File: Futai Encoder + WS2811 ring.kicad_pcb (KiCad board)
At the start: 2 copper layers, 31 x 49 mm, 41 parts, among them J1 Conn_02x05_Top_Bottom, SW1 RotaryEncoder_Switch_RGB

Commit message: new 3d for encoder, fixing ibom.html + new images
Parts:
- C1, C10, C4, C7: value 33n -> 100n

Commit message: adding v0.7
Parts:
- added kibuzzard-61E72360: G***, kibuzzard-61E72360, B.Cu at (148.6, 99.2)
- D1, D10, D11, D12, D2, D3, D4, D5, D6, D7, D8, D9: footprint footprints:WS2811-THT-LED -> andilge KiCad footprints:WS2811D-F5-1261
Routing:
- net Net-(D11-Pad2): track 5.51 -> 4.10 mm
- net Net-(D3-Pad2): track 7.47 -> 6.39 mm
- net Net-(D8-Pad2): track 8.51 -> 7.45 mm
- net Net-(D9-Pad2): track 7.63 -> 6.60 mm
- net +5V: track 154.3 -> 153.6 mm
- net ENC_A: track 28.4 -> 27.8 mm
- net ENC_B: track 43.4 -> 42.8 mm
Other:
- board text added: "v0.7"
- board text removed: "by andilge"
- board text removed: "v0.65"

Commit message: adding fabrication files for 0.7
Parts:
- D1, D10, D11, D12, D2, D3, D4, D5, D6, D7, D8, D9: value WS2812D -> WS2812D F5 hat

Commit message: lowering value for R1-R12
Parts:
- R1, R10, R11, R12, R2, R3, R4, R5, R6, R7, R8, R9: value 130 -> 68
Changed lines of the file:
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@@
       (drillshape 0)
       (scaleselection 1)
-      (outputdirectory "gerber-and-bom/")
+      (outputdirectory "fabrication/")
     )
   )
@@
     (descr "Through hole straight pin header, 1x03, 2.54mm pitch, single row")
     (tags "Through hole pin header THT 1x03 2.54mm single row")
-    (property "Purchse" "https://www.aliexpress.com/item/32790928817.html")
+    (property "Purchase" "https://www.aliexpress.com/item/32790928817.html")
     (property "Sheetfile" "Futai Encoder + WS2811 ring.kicad_sch")
     (property "Sheetname" "")
@@
     (descr "Through hole straight pin header, 1x03, 2.54mm pitch, single row")
     (tags "Through hole pin header THT 1x03 2.54mm single row")
-    (property "Purchse" "https://www.aliexpress.com/item/32790928817.html")
+    (property "Purchase" "https://www.aliexpress.com/item/32790928817.html")
     (property "Sheetfile" "Futai Encoder + WS2811 ring.kicad_sch")
     (property "Sheetname" "")
@@
       (effects (font (size 1 1) (thickness 0.15)) (justify mirror))
     )
-    (fp_text value "130" (at 0 -1.65 90) (layer "B.Fab")
+    (fp_text value "68" (at 0 -1.65 90) (layer "B.Fab")
       (effects (font (size 1 1) (thickness 0.15)) (justify mirror))
     )
@@
       (effects (font (size 1 1) (thickness 0.15)) (justify mirror))
     )
-    (fp_text value "130" (at 0 -1.65) (layer "B.Fab")
+    (fp_text value "68" (at 0 -1.65) (layer "B.Fab")
       (effects (font (size 1 1) (thickness 0.15)) (justify mirror))
     )
@@
       (effects (font (size 1 1) (thickness 0.15)) (justify mirror))
     )
-    (fp_text value "130" (at 0 -1.65 90) (layer "B.Fab")
+    (fp_text value "68" (at 0 -1.65 90) (layer "B.Fab")
       (effects (font (size 1 1) (thickness 0.15)) (justify mirror))
     )
@@
       (effects (font (size 1 1) (thickness 0.15)) (justify mirror))
     )
-    (fp_text value "130" (at 0 -1.65 270) (layer "B.Fab")
+    (fp_text value "68" (at 0 -1.65 270) (layer "B.Fab")
       (effects (font (size 1 1) (thickness 0.15)) (justify mirror))
     )
@@
       (effects (font (size 1 1) (thickness 0.15)) (justify mirror))
     )
-    (fp_text value "130" (at 0 -1.65 180) (layer "B.Fab")
+    (fp_text value "68" (at 0 -1.65 180) (layer "B.Fab")
       (effects (font (size 1 1) (thickness 0.15)) (justify mirror))
     )
@@
       (effects (font (size 1 1) (thickness 0.15)) (justify mirror))
     )
-    (fp_text value "130" (at 0 -1.65 90) (layer "B.Fab")
+    (fp_text value "68" (at 0 -1.65 90) (layer "B.Fab")
       (effects (font (size 1 1) (thickness 0.15)) (justify mirror))
     )
@@
       (effects (font (size 1 1) (thickness 0.15)) (justify mirror))
     )
-    (fp_text value "130" (at 0 -1.65 270) (layer "B.Fab")
+    (fp_text value "68" (at 0 -1.65 270) (layer "B.Fab")
       (effects (font (size 1 1) (thickness 0.15)) (justify mirror))
     )
@@
       (effects (font (size 1 1) (thickness 0.15)) (justify mirror))
     )
-    (fp_text value "130" (at 0 -1.65 180) (layer "B.Fab")
+    (fp_text value "68" (at 0 -1.65 180) (layer "B.Fab")
       (effects (font (size 1 1) (thickness 0.15)) (justify mirror))
     )
@@
       (effects (font (size 1 1) (thickness 0.15)) (justify mirror))
     )
-    (fp_text value "130" (at 0 -1.65 90) (layer "B.Fab")
+    (fp_text value "68" (at 0 -1.65 90) (layer "B.Fab")
       (effects (font (size 1 1) (thickness 0.15)) (justify mirror))
     )
@@
       (effects (font (size 1 1) (thickness 0.15)) (justify mirror))
     )
-    (fp_text value "130" (at 0 -1.65 270) (layer "B.Fab")
+    (fp_text value "68" (at 0 -1.65 270) (layer "B.Fab")
       (effects (font (size 1 1) (thickness 0.15)) (justify mirror))
     )
@@
     (descr "Capacitor SMD 0805 (2012 Metric), square (rectangular) end terminal, IPC_7351 nominal, (Body size source: IPC-SM-782 page 76, https://www.pcb-3d.com/wordpress/wp-content/uploads/ipc-sm-782a_amendment_1_and_2.pdf, https://docs.google.com/spreadsheets/d/1BsfQQcO9C6DZCsRaXUlFlo91Tg2WpOkGARC1WS5S8t0/edit?usp=sharing), generated with kicad-footprint-generator")
     (tags "capacitor")
-    (property "Puchase" "https://www.aliexpress.com/item/32964553793.html")
+    (property "Purchase" "https://www.aliexpress.com/item/32964553793.html")
     (property "Sheetfile" "Futai Encoder + WS2811 ring.kicad_sch")
     (property "Sheetname" "")
@@
       (effects (font (size 1 1) (thickness 0.15)) (justify mirror))
     )
-    (fp_text value "130" (at 0 -1.65) (layer "B.Fab")
+    (fp_text value "68" (at 0 -1.65) (layer "B.Fab")
       (effects (font (size 1 1) (thickness 0.15)) (justify mirror))
     )
@@
       (effects (font (size 1 1) (thickness 0.15)) (justify mirror))
     )
-    (fp_text value "130" (at 0 -1.65 270) (layer "B.Fab")
-      (effects (font (size 1 1) (thickness 0.15)) (justify mirror))
-    )
+    (fp_text value "68" (at 0 -1.65 270) (layer "B.Fab")
+      (effects (font (size 1 1) (thickness 0.15)) (justify mirror))
+    )

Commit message: small change to value R1-R12
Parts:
- R1, R10, R11, R12, R2, R3, R4, R5, R6, R7, R8, R9: value 68 -> 62
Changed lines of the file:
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@@
       (effects (font (size 1 1) (thickness 0.15)) (justify mirror))
     )
-    (fp_text value "68" (at 0 -1.65 90) (layer "B.Fab")
+    (fp_text value "62" (at 0 -1.65 90) (layer "B.Fab")
       (effects (font (size 1 1) (thickness 0.15)) (justify mirror))
     )
@@
       (effects (font (size 1 1) (thickness 0.15)) (justify mirror))
     )
-    (fp_text value "68" (at 0 -1.65) (layer "B.Fab")
+    (fp_text value "62" (at 0 -1.65) (layer "B.Fab")
       (effects (font (size 1 1) (thickness 0.15)) (justify mirror))
     )
@@
       (effects (font (size 1 1) (thickness 0.15)) (justify mirror))
     )
-    (fp_text value "68" (at 0 -1.65 90) (layer "B.Fab")
+    (fp_text value "62" (at 0 -1.65 90) (layer "B.Fab")
       (effects (font (size 1 1) (thickness 0.15)) (justify mirror))
     )
@@
       (effects (font (size 1 1) (thickness 0.15)) (justify mirror))
     )
-    (fp_text value "68" (at 0 -1.65 270) (layer "B.Fab")
+    (fp_text value "62" (at 0 -1.65 270) (layer "B.Fab")
       (effects (font (size 1 1) (thickness 0.15)) (justify mirror))
     )
@@
       (effects (font (size 1 1) (thickness 0.15)) (justify mirror))
     )
-    (fp_text value "68" (at 0 -1.65 180) (layer "B.Fab")
+    (fp_text value "62" (at 0 -1.65 180) (layer "B.Fab")
       (effects (font (size 1 1) (thickness 0.15)) (justify mirror))
     )
@@
       (effects (font (size 1 1) (thickness 0.15)) (justify mirror))
     )
-    (fp_text value "68" (at 0 -1.65 90) (layer "B.Fab")
+    (fp_text value "62" (at 0 -1.65 90) (layer "B.Fab")
       (effects (font (size 1 1) (thickness 0.15)) (justify mirror))
     )
@@
       (effects (font (size 1 1) (thickness 0.15)) (justify mirror))
     )
-    (fp_text value "68" (at 0 -1.65 270) (layer "B.Fab")
+    (fp_text value "62" (at 0 -1.65 270) (layer "B.Fab")
       (effects (font (size 1 1) (thickness 0.15)) (justify mirror))
     )
@@
       (effects (font (size 1 1) (thickness 0.15)) (justify mirror))
     )
-    (fp_text value "68" (at 0 -1.65 180) (layer "B.Fab")
+    (fp_text value "62" (at 0 -1.65 180) (layer "B.Fab")
       (effects (font (size 1 1) (thickness 0.15)) (justify mirror))
     )
@@
       (effects (font (size 1 1) (thickness 0.15)) (justify mirror))
     )
-    (fp_text value "68" (at 0 -1.65 90) (layer "B.Fab")
+    (fp_text value "62" (at 0 -1.65 90) (layer "B.Fab")
       (effects (font (size 1 1) (thickness 0.15)) (justify mirror))
     )
@@
       (effects (font (size 1 1) (thickness 0.15)) (justify mirror))
     )
-    (fp_text value "68" (at 0 -1.65 270) (layer "B.Fab")
+    (fp_text value "62" (at 0 -1.65 270) (layer "B.Fab")
       (effects (font (size 1 1) (thickness 0.15)) (justify mirror))
     )
@@
       (effects (font (size 1 1) (thickness 0.15)) (justify mirror))
     )
-    (fp_text value "68" (at 0 -1.65) (layer "B.Fab")
+    (fp_text value "62" (at 0 -1.65) (layer "B.Fab")
       (effects (font (size 1 1) (thickness 0.15)) (justify mirror))
     )
@@
       (effects (font (size 1 1) (thickness 0.15)) (justify mirror))
     )
-    (fp_text value "68" (at 0 -1.65 270) (layer "B.Fab")
-      (effects (font (size 1 1) (thickness 0.15)) (justify mirror))
-    )
+    (fp_text value "62" (at 0 -1.65 270) (layer "B.Fab")
+      (effects (font (size 1 1) (thickness 0.15)) (justify mirror))
+    )

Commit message: v0.8
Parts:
- removed C10, C4: 100n, Capacitor_SMD:C_0805_2012Metric
- removed R12: 62, Resistor_SMD:R_0805_2012Metric
- removed kibuzzard-61E72360: G***, kibuzzard-61E72360
- added C11: 220n, Capacitor_SMD:C_0805_2012Metric, B.Cu at (145.2, 93.6)
- added C3: 220n, Capacitor_SMD:C_0805_2012Metric, B.Cu at (159.4, 110.5)
- added C5: 220n, Capacitor_SMD:C_0805_2012Metric, B.Cu at (151.6, 106.0)
- added C9: 220n, Capacitor_SMD:C_0805_2012Metric, B.Cu at (135.0, 86.2)
- added kibuzzard-61E92DF0: G***, kibuzzard-61E92DF0, B.Cu at (148.4, 99.2)
- C1, C7: value 100n -> 220n
- R1, R10, R11, R2, R3, R4, R5, R6, R7, R8, R9: value 62 -> 75
- moved R2 10.8 mm to (159.1, 99.2), turned to 90 degrees
- moved R8 10.3 mm to (137.9, 99.2), turned to -90 degrees
- moved R10 7.55 mm to (143.3, 89.8), turned to 30 degrees
- moved R4 7.39 mm to (153.8, 108.4), turned to -150 degrees
- moved R1 7.37 mm to (157.7, 94.0), turned to 120 degrees
- moved R9 7.03 mm to (139.3, 93.9), turned to -120 degrees
- moved R7 6.98 mm to (139.3, 104.4), turned to -60 degrees
- moved R3 6.71 mm to (157.7, 104.4), turned to 60 degrees
- moved C1 3.92 mm to (162.0, 87.4), turned to 0 degrees
- moved R11 3.66 mm to (148.9, 88.5), turned to 0 degrees
- moved R5 3.29 mm to (148.4, 109.7), turned to 180 degrees
- moved C7 3.13 mm to (137.3, 109.5)
- moved R6 2.76 mm to (143.2, 108.3), turned to 150 degrees
- moved C31 1.00 mm to (143.3, 69.9)
- moved R31 1.00 mm to (143.3, 73.9)
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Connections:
- C1 pad 1: Net-(C1-Pad1) -> +5VL
- C7 pad 1: Net-(C7-Pad1) -> +5VL
- D1 pad 2: Net-(C1-Pad1) -> +5VL
- D10 pad 2: Net-(C10-Pad1) -> +5VL
- D11 pad 2: Net-(D11-Pad2) -> +5VL
- D11 pad 4: Net-(D10-Pad1) -> Net-(D11-Pad4)
- D12 pad 2: Net-(D12-Pad2) -> +5VL
- D12 pad 4: Net-(D11-Pad1) -> Net-(D12-Pad4)
- D2 pad 2: Net-(D2-Pad2) -> +5VL
- D2 pad 4: Net-(D1-Pad1) -> Net-(D2-Pad4)
- D3 pad 2: Net-(D3-Pad2) -> +5VL
- D3 pad 4: Net-(D2-Pad1) -> Net-(D3-Pad4)
- D4 pad 2: Net-(C4-Pad2) -> +5VL
- D4 pad 4: Net-(D3-Pad1) -> Net-(D4-Pad4)
- D5 pad 2: Net-(D5-Pad2) -> +5VL
- D5 pad 4: Net-(D4-Pad1) -> Net-(D5-Pad4)
- D6 pad 2: Net-(D6-Pad2) -> +5VL
- D6 pad 4: Net-(D5-Pad1) -> Net-(D6-Pad4)
- D7 pad 2: Net-(C7-Pad1) -> +5VL
- D7 pad 4: Net-(D6-Pad1) -> Net-(D7-Pad4)
- D8 pad 2: Net-(D8-Pad2) -> +5VL
- D8 pad 4: Net-(D7-Pad1) -> Net-(D8-Pad4)
- D9 pad 1: Net-(D10-Pad4) -> Net-(D9-Pad1)
- D9 pad 2: Net-(D9-Pad2) -> +5VL
- D9 pad 4: Net-(D8-Pad1) -> Net-(D9-Pad4)
- J1 pad 5: +5V -> +5VL
- R1 pad 1: +5V -> Net-(D2-Pad4)
- R1 pad 2: Net-(C1-Pad1) -> Net-(D1-Pad1)
- R10 pad 1: +5V -> Net-(D10-Pad1)
- R10 pad 2: Net-(C10-Pad1) -> Net-(D11-Pad4)
- R11 pad 1: +5V -> Net-(D11-Pad1)
- R11 pad 2: Net-(D11-Pad2) -> Net-(D12-Pad4)
- R2 pad 1: +5V -> Net-(D3-Pad4)
- R2 pad 2: Net-(D2-Pad2) -> Net-(D2-Pad1)
- R3 pad 1: +5V -> Net-(D4-Pad4)
- R3 pad 2: Net-(D3-Pad2) -> Net-(D3-Pad1)
- R31 pad 1: +5V -> +5VL
- R4 pad 1: +5V -> Net-(D4-Pad1)
- R4 pad 2: Net-(C4-Pad2) -> Net-(D5-Pad4)
- R41 pad 1: +5V -> +5VL
- R5 pad 1: +5V -> Net-(D5-Pad1)
- R5 pad 2: Net-(D5-Pad2) -> Net-(D6-Pad4)
- R6 pad 1: +5V -> Net-(D6-Pad1)
- R6 pad 2: Net-(D6-Pad2) -> Net-(D7-Pad4)
- R7 pad 1: +5V -> Net-(D8-Pad4)
- R7 pad 2: Net-(C7-Pad1) -> Net-(D7-Pad1)
- R8 pad 1: +5V -> Net-(D9-Pad4)
- R8 pad 2: Net-(D8-Pad2) -> Net-(D8-Pad1)
- R9 pad 1: +5V -> Net-(D10-Pad4)
- R9 pad 2: Net-(D9-Pad2) -> Net-(D9-Pad1)
- SW1 pad 1: +5V -> +5VL
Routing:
- net +5VL: track 0.00 -> 215.0 mm, vias 0 -> 10
- net +5V: track 153.6 -> 0.00 mm, vias 6 -> 0
- net Net-(D2-Pad2): track 9.12 -> 0.00 mm
- net Net-(D8-Pad2): track 7.45 -> 0.00 mm
- net Net-(C1-Pad1): track 6.60 -> 0.00 mm
- net Net-(D9-Pad2): track 6.60 -> 0.00 mm
- net Net-(D3-Pad2): track 6.39 -> 0.00 mm
- net Net-(C7-Pad1): track 6.22 -> 0.00 mm
- net Net-(C10-Pad1): track 6.11 -> 0.00 mm
- net Net-(D6-Pad2): track 6.02 -> 0.00 mm
- net Net-(D5-Pad2): track 5.83 -> 0.00 mm
- net Net-(D12-Pad2): track 5.47 -> 0.00 mm
- net Net-(C4-Pad2): track 5.44 -> 0.00 mm
- net Net-(D11-Pad2): track 4.10 -> 0.00 mm
- net Net-(D4-Pad4): track 0.00 -> 2.63 mm
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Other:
- board text added: "v0.8"
- board text removed: "v0.7"

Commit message: v0.9
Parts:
- removed kibuzzard-61E92DF0: G***, kibuzzard-61E92DF0
- added R51: 15k, Resistor_SMD:R_0805_2012Metric, B.Cu at (152.5, 93.3)
- added R52: 2k, Resistor_SMD:R_0805_2012Metric, B.Cu at (152.5, 95.5)
- added R61: 15k, Resistor_SMD:R_0805_2012Metric, B.Cu at (144.4, 96.7)
- added R62: 2k, Resistor_SMD:R_0805_2012Metric, B.Cu at (144.4, 98.8)
- added R71: 15k, Resistor_SMD:R_0805_2012Metric, B.Cu at (152.3, 98.8)
- added R72: 2k, Resistor_SMD:R_0805_2012Metric, B.Cu at (152.3, 101.0)
- added R81: 100, Resistor_SMD:R_0805_2012Metric, B.Cu at (152.3, 103.1)
- added kibuzzard-61EB43D1: G***, kibuzzard-61EB43D1, B.Cu at (148.6, 82.5)
- moved C21 9.77 mm to (158.8, 86.8), turned to 180 degrees
- moved R22 9.71 mm to (156.3, 82.6)
- moved R21 8.55 mm to (158.8, 84.7), turned to 180 degrees
- moved C9 4.45 mm to (139.3, 85.0), turned to 90 degrees
- moved R33 3.09 mm to (143.2, 70.9)
- moved R43 3.08 mm to (153.7, 70.9)
- moved C1 1.71 mm to (161.7, 85.7), turned to 90 degrees
- moved R10 1.19 mm to (143.5, 91.0), turned to 0 degrees
- moved R31 1.09 mm to (143.2, 75.0)
- moved R32 1.07 mm to (143.2, 73.0)
- moved C7 1.07 mm to (137.5, 110.5)
- moved R41 1.06 mm to (153.7, 75.0)
- moved R42 1.06 mm to (153.7, 73.0)
- moved C41 1.06 mm to (153.7, 68.8)
- moved C31 1.04 mm to (143.2, 68.8)
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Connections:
- J1 pad 6: RED -> Q-RED
- J1 pad 7: GRE -> Q-GRE
- J1 pad 8: BLU -> Q-BLU
- SW1 pad 1: +5VL -> Net-(R81-Pad2)
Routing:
- net Q-BLU: track 0.00 -> 38.2 mm, vias 0 -> 1
- net BLU: track 41.8 -> 4.51 mm, vias 2 -> 0
- net +5VL: track 215.0 -> 178.1 mm, vias 10 -> 2
- net Q-GRE: track 0.00 -> 30.0 mm, vias 0 -> 1
- net RED: track 31.5 -> 4.43 mm, vias 2 -> 0
- net Q-RED: track 0.00 -> 23.4 mm, vias 0 -> 1
- net GRE: track 32.1 -> 12.7 mm
- net ENC_B: track 43.1 -> 49.3 mm, vias 1 -> 4
- net Net-(C21-Pad1): track 14.6 -> 18.3 mm
- net SWC: track 20.4 -> 16.9 mm, vias 2 -> 0
- net GND: track 3.29 -> 5.90 mm, vias 33 -> 21
- net Net-(R81-Pad2): track 0.00 -> 2.30 mm
- net DOUT: track 14.4 -> 12.2 mm, vias 0 -> 1
- net Net-(D11-Pad4): track 2.36 -> 4.08 mm
- net DIN: track 14.1 -> 15.1 mm, vias 0 -> 1
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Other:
- board text added: "SW"
- board text added: "v0.9"
- board text removed: "SWC"
- board text removed: "v0.8"

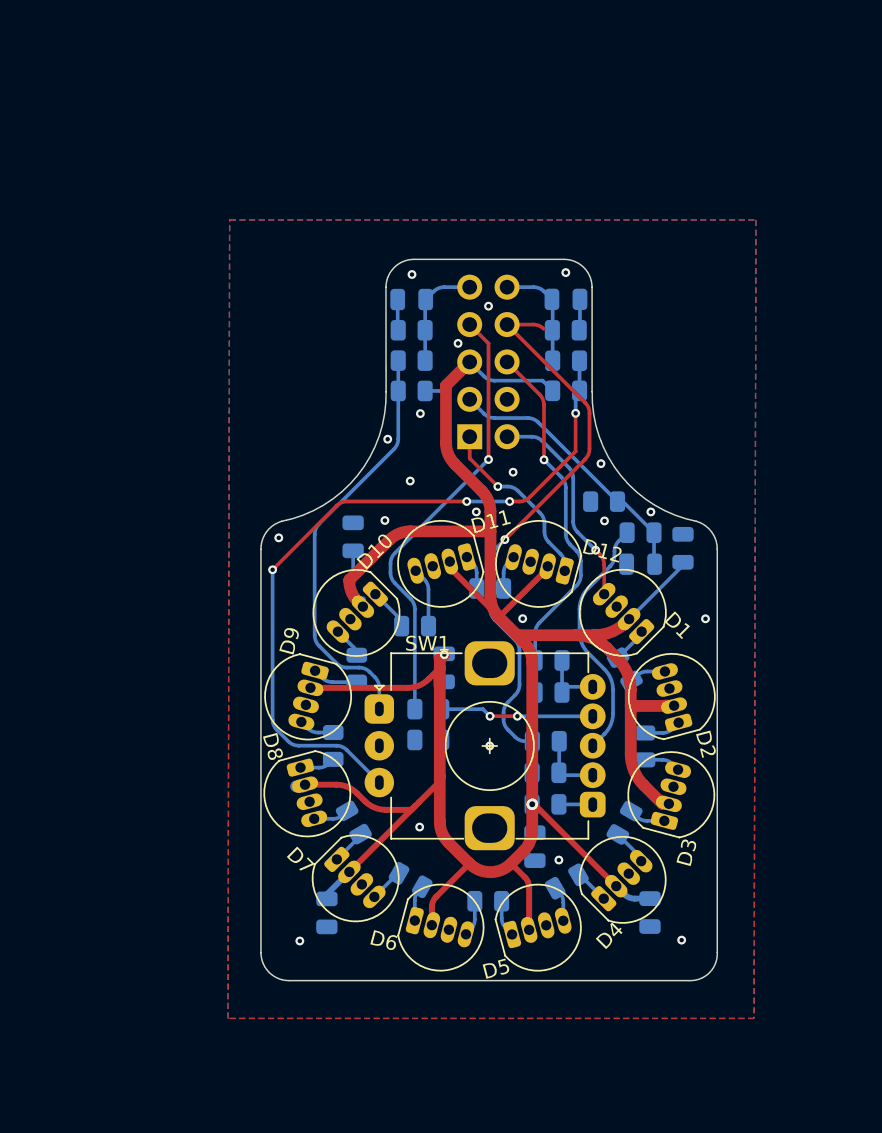
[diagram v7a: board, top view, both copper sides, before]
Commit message: better edge cut, adding more info to README.md
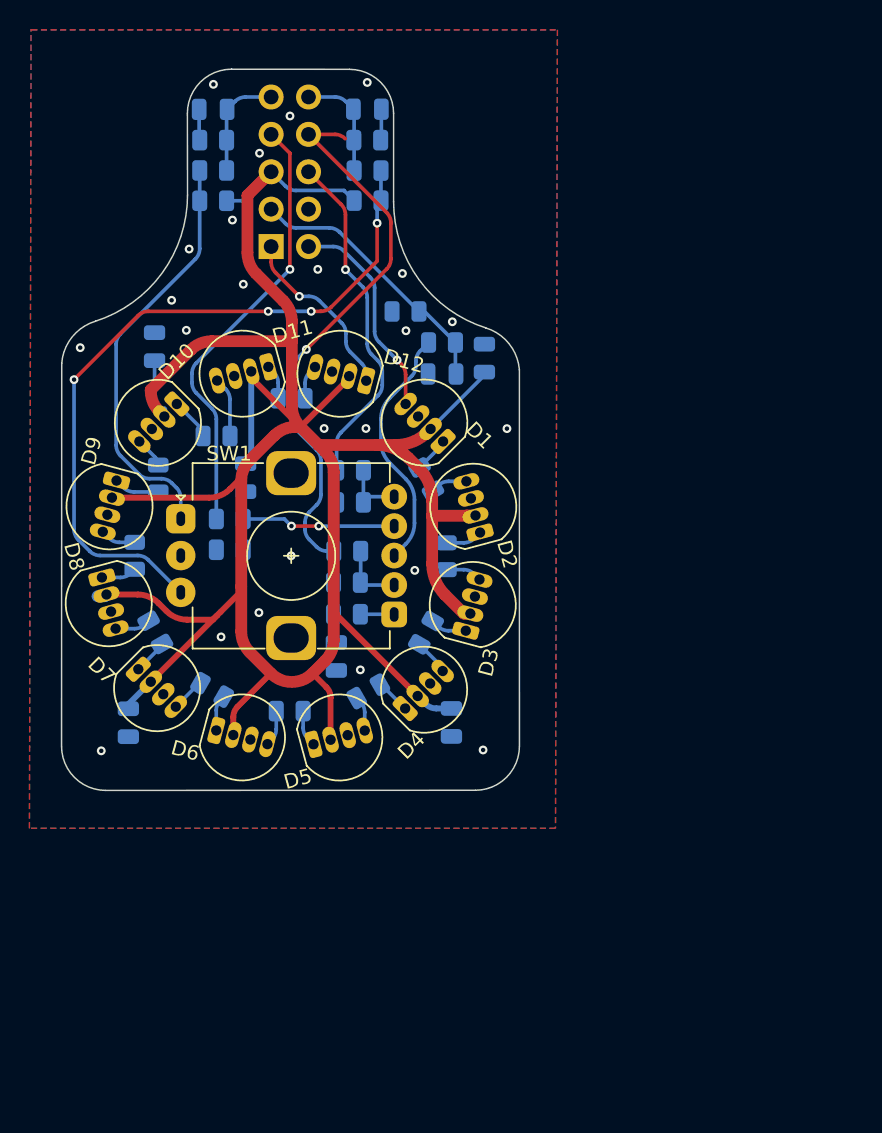
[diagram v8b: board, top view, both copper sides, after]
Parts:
- R51, R61, R71: value 15k -> 12k
- moved R31 18.7 mm to (129.8, 62.1)
- moved C3 18.7 mm to (145.9, 97.6)
- moved C31 18.7 mm to (129.8, 55.9)
- moved C5 18.7 mm to (138.1, 93.1)
- moved D1 18.7 mm to (144.1, 77.2)
- moved D11 18.7 mm to (131.8, 73.9)
- moved D12 18.7 mm to (138.4, 73.9)
- moved D2 18.7 mm to (147.4, 82.9)
- moved D3 18.7 mm to (147.4, 89.6)
- moved D4 18.7 mm to (144.1, 95.3)
- moved D5 18.7 mm to (138.3, 98.6)
- moved D6 18.7 mm to (131.7, 98.6)
- moved D7 18.7 mm to (125.9, 95.2)
- moved D8 18.7 mm to (122.7, 89.5)
- moved D9 18.7 mm to (122.7, 82.9)
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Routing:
- net +5VL: track 178.1 -> 197.0 mm, vias 2 -> 0
- net GND: vias 21 -> 24
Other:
- board size 31 x 49 mm -> 31.1 x 49 mm
